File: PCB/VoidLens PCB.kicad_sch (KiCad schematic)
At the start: 72 parts, among them IC1 BMI270, J1 solder pad, J2 JST-XH-2 Pin, J3 USB4105-GF-A, J4 JST_XH for led Strip, J5 Programming_Pins, J6 power jumper, Q1 MMBT3904-E, Q2 DXT2011P5-13, SW1 SW_SPST, SW2 SW_Push, SW3 SW_SPDT, SW4 SW_Push, U1 BQ24074RGT, U2 ATmega32U4-A, U3 NRF24L01, U5 TPS61022, U6 TPS27081ADDCR, Y1 16Mhz, Y2 16mhz

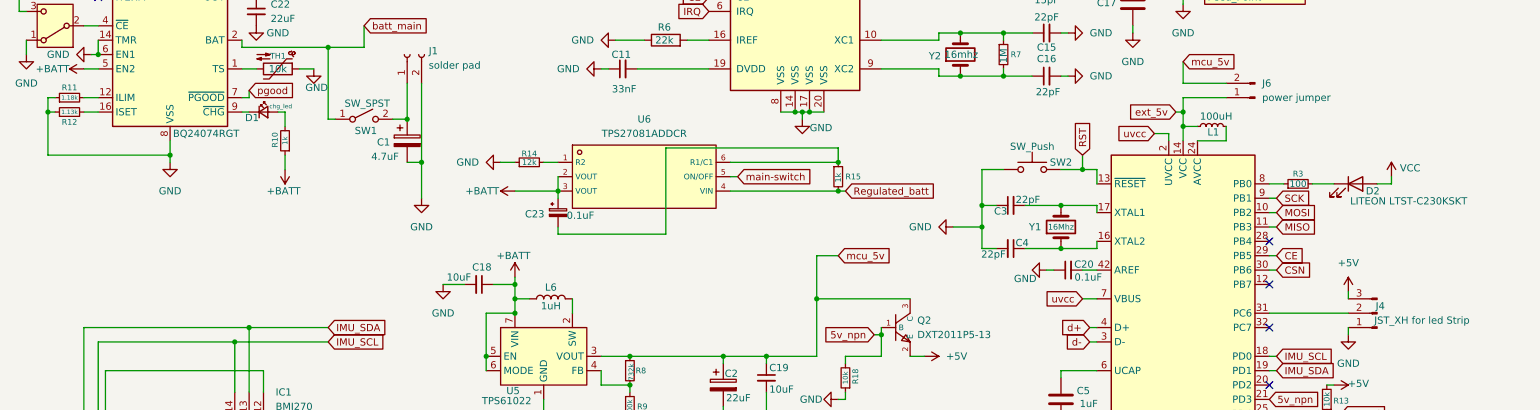
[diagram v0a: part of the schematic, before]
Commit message: assigned some more footprints
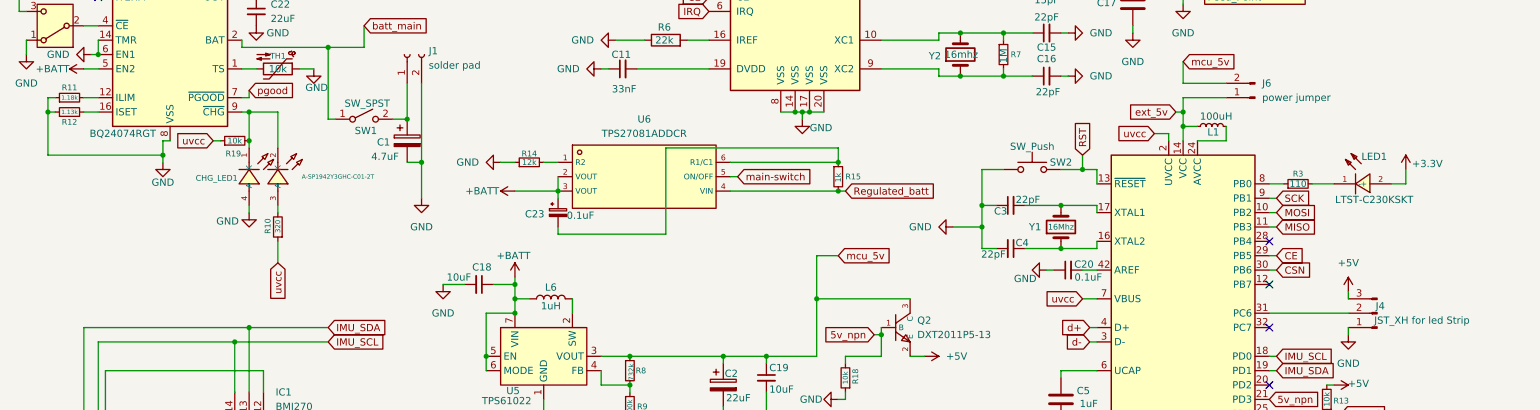
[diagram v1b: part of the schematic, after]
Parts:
- removed D1: chg_led, symbol Device:LED_Small
- removed D2: LITEON LTST-C230KSKT, symbol Device:LED
- added CHG_LED1: A-SP1942Y3GHC-C01-2T, lcsc_footprints:C19171267_LED-SMD_4P-L1_6-W1_5_A-SP1942Y3GHC-C01-2T, symbol lcsc_imported:A-SP1942Y3GHC-C01-2T
- added LED1: LTST-C230KSKT, lcsc_footprints:C125108_LED1206-RD_YELLOW-SIDE, symbol lcsc_imported:LTST-C230KSKT
- added R19: 10k, symbol Device:R_Small
- C20, C23: footprint (none) -> Capacitor_SMD:C_0603_1608Metric_Pad1.08x0.95mm_HandSolder
- IC1: footprint (none) -> Package_LGA:Bosch_LGA-14_3x2.5mm_P0.5mm
- J1: footprint (none) -> Solder_Pads:01x02 Solder Pad 3mm Dia, 2mm Spacing
- J2: footprint (none) -> Connector_JST:JST_XH_B2B-XH-A_1x02_P2.50mm_Vertical
- R10: value 1k -> 320
- R3: value 100 -> 110
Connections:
- net +3.3V: now also LED1.2 (+)
- net +BATT: no longer R10.1
- net GND: now also CHG_LED1.4 (A)
- net VBUS: now also R10.1, R19.1
- net at R3.2: now also LED1.1 (-)
- net at U1.9 (~{CHG}): now also CHG_LED1.1 (K), CHG_LED1.2 (K), R19.2
- net at R10.2: now also CHG_LED1.3 (A)
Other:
- moved on the sheet: R10
